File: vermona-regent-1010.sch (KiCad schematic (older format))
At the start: 0 parts

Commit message: Start drawing schematics
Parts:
- added C?: C, symbol Device:C
- added J?: Input, symbol Connector_Generic:Conn_01x02
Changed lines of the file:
@@
 encoding utf-8
 Sheet 1 1
-Title ""
-Date "2021-06-09"
-Rev ""
-Comp ""
+Title "Vermona Regent 1010"
+Date "2021-06-16"
+Rev "0.1"
+Comp "Радиохобби 6/2010"
 Comment1 ""
 Comment2 ""
@@
 Comment4 ""
 $EndDescr
+$Comp
+L Connector_Generic:Conn_01x02 J?
+U 1 1 60C93D53
+P 1200 2800
+F 0 "J?" H 1118 3017 50  0000 C CNN
+F 1 "Input" H 1118 2926 50  0000 C CNN
+F 2 "" H 1200 2800 50  0001 C CNN
+F 3 "~" H 1200 2800 50  0001 C CNN
+	1    1200 2800
+	-1   0    0    -1
+$EndComp
+$Comp
+L Device:C C?
+U 1 1 60C94D66
+P 1850 2800
+F 0 "C?" V 2102 2800 50  0000 C CNN
+F 1 "C" V 2011 2800 50  0000 C CNN
+F 2 "" H 1888 2650 50  0001 C CNN
+F 3 "~" H 1850 2800 50  0001 C CNN
+	1    1850 2800
+	0    -1   -1   0
+$EndComp
 $EndSCHEMATC

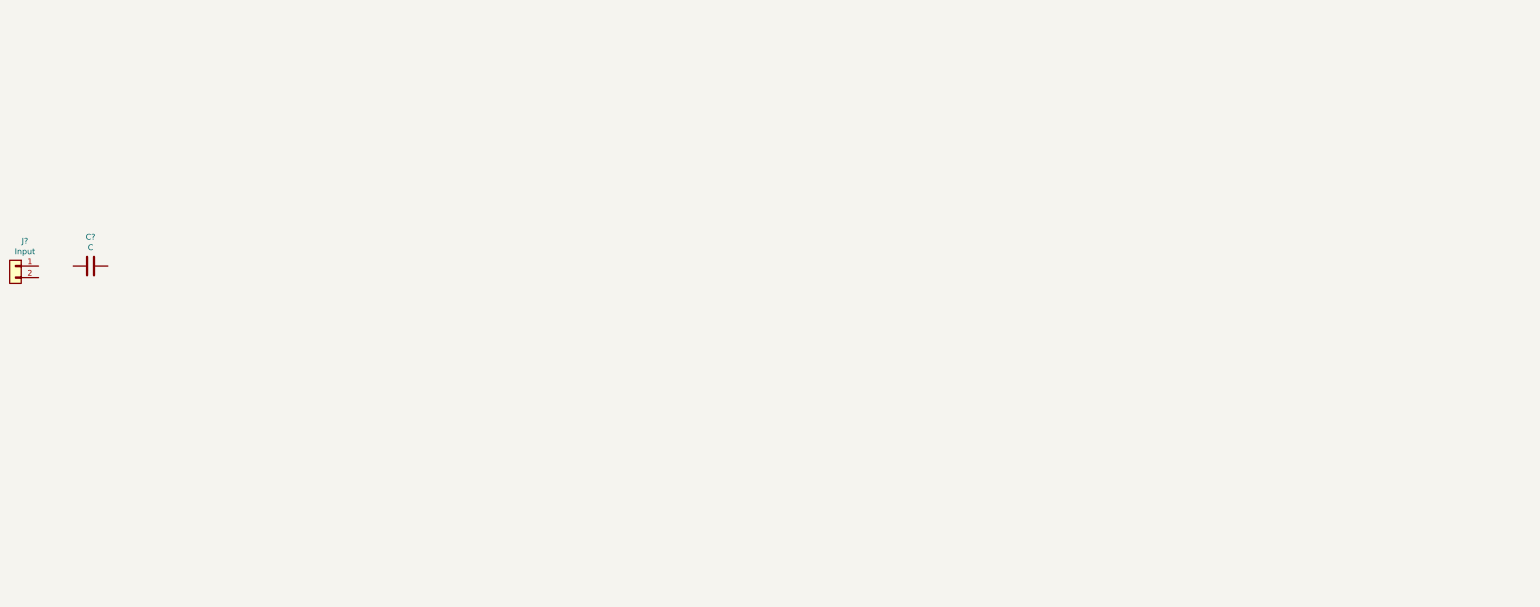
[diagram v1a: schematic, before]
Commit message: Draw lower shoulder
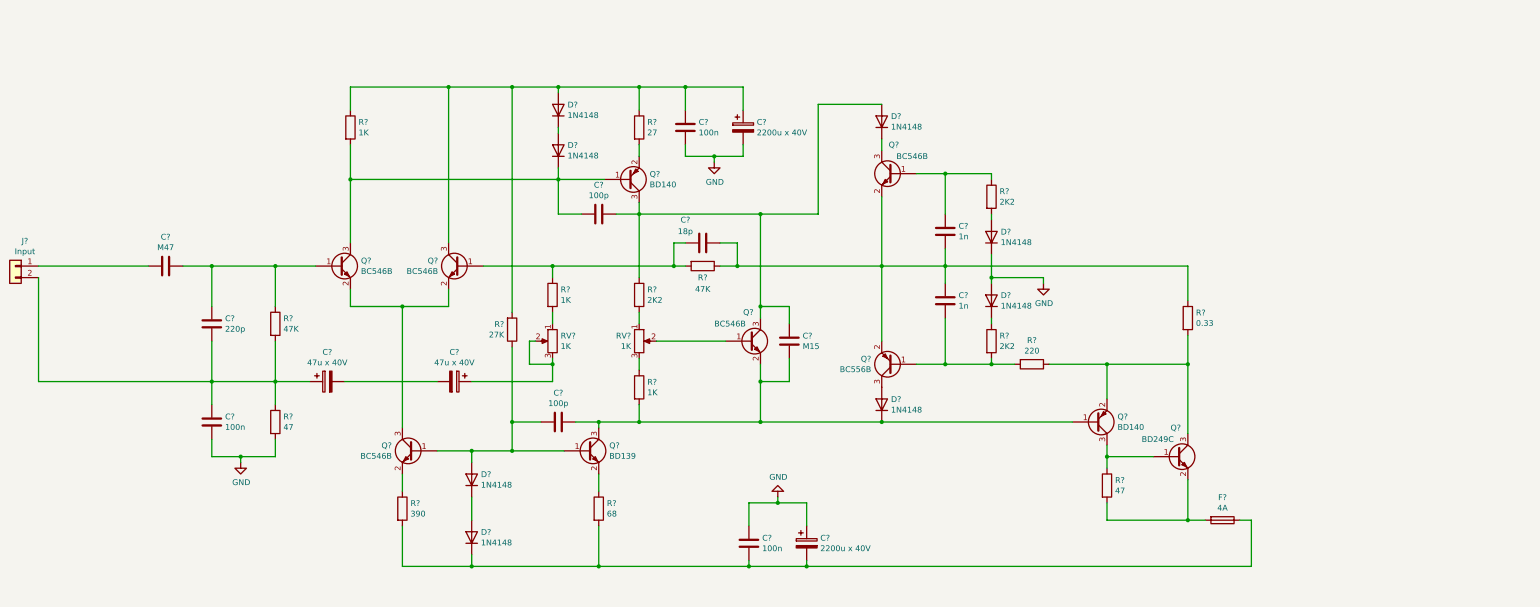
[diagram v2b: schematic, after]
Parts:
- added C?: 220p, symbol Device:C
- added C? (x3): 100n, symbol Device:C
- added C? (x2): 47u x 40V, symbol Device:CP
- added C? (x2): 100p, symbol Device:C
- added C? (x2): 2200u x 40V, symbol Device:CP
- added C?: 18p, symbol Device:C
- added C?: M15, symbol Device:C
- added C? (x2): 1n, symbol Device:C
- added D? (x8): 1N4148, symbol Device:D
- added F?: 4A, symbol Device:Fuse
- added Q? (x5): BC546B, symbol Device:Q_NPN_BEC
- added Q?: BD139, symbol Device:Q_NPN_BEC
- added Q? (x2): BD140, symbol Device:Q_PNP_BEC
- added Q?: BC556B, symbol Device:Q_PNP_BEC
- added Q?: BD249C, symbol Device:Q_NPN_BEC
- added R? (x2): 47K, symbol Device:R
- added R? (x2): 47, symbol Device:R
- added R?: 390, symbol Device:R
- added R? (x3): 1K, symbol Device:R
- added R?: 27K, symbol Device:R
- added R?: 68, symbol Device:R
- added R?: 27, symbol Device:R
- added R? (x3): 2K2, symbol Device:R
- added R?: 220, symbol Device:R
- added R?: 0.33, symbol Device:R
- added RV? (x2): 1K, symbol Device:R_POT
- C?: value C -> M47
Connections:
- net at J?.1 (Pin_1): now also C?.1
- net at J?.2 (Pin_2): now also C?.1, C?.1, C?.2, R?.1, R?.2
- net at C?.2: now also C?.1, Q?.1 (B), R?.1
- new net: Q?.2 (E), Q?.2 (E), Q?.3 (C)
- new net: C?.1, D?.1 (K), Q?.1 (B), Q?.3 (C), R?.2
- new net: C?.2, Q?.1 (B), R?.1, R?.2
- new net: C?.1, C?.1, D?.2 (A), Q?.3 (C), R?.1, R?.1, R?.2
- new net: C?.2, C?.2
- new net: C?.1, RV?.2, RV?.3
- new net: C?.2, D?.2 (A), Q?.1 (B), Q?.1 (B), R?.1
- new net: Q?.2 (E), R?.1 (x2)
- new net: C?.2, C?.2, D?.1 (K), F?.1, R?.2, R?.2
- new net: D?.1 (K), D?.2 (A) (x2)
- new net: C?.1, C?.2, D?.1 (K), Q?.1 (B), Q?.2 (E), Q?.3 (C), R?.2
- new net: R?.2, RV?.1 (x2)
- new net: Q?.2 (E), R?.2
- new net: C?.1, C?.2, D?.2 (A), Q?.3 (C), Q?.3 (C), R?.1
- new net: Q?.1 (B), RV?.2
- new net: R?.1, RV?.3
- new net: C?.1, C?.1, C?.2, Q?.2 (E), Q?.2 (E), R?.1, R?.1
- new net: D?.1 (K), Q?.3 (C)
- new net: C?.1, Q?.1 (B), R?.1
- new net: C?.2, Q?.1 (B), R?.2, R?.2
- new net: D?.2 (A), Q?.3 (C)
- new net: D?.2 (A), R?.2
- new net: D?.1 (K), R?.1
- new net: Q?.2 (E), Q?.3 (C), R?.1, R?.2
- new net: Q?.1 (B), Q?.3 (C), R?.1
- new net: F?.2, Q?.2 (E), R?.2
- new net GND: C?.1, C?.1, C?.2, C?.2, C?.2, D?.1 (K), D?.2 (A), R?.2
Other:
- moved on the sheet: C?

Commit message: Finish schematics
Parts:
- added C16: 100n, symbol Device:C
- added F1: 4A, symbol Device:Fuse
- added LS1: 100W x 4 Ohm, symbol Device:Speaker
- added Q11: КТ819ГМ, symbol Device:Q_NPN_BEC
- added Q9: КТ815Г, symbol Device:Q_NPN_BEC
- added R14: 220, symbol Device:R
- added R16: 47, symbol Device:R
- added R18: 0.33, symbol Device:R
- added R20: 10, symbol Device:R
- Q1, Q2, Q3, Q6, Q7: renamed from Q?; value BC546B -> КТ3102Б
- Q10, Q5: renamed from Q?; value BD140 -> КТ814Г
- Q12: renamed from Q?; value BD249C -> КТ819ГМ
- Q4: renamed from Q?; value BD139 -> КТ815Г
- Q8: renamed from Q?; value BC556B -> КТ502Д
- gave numbers to parts that had none: 43
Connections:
- net GND: now also C16.2, LS1.2
- net at C10.1, C8.1, D3.2 (A)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: now also F1.2, Q11.3 (C), Q9.3 (C)
- net -40V: now reaches C11.2, C13.2, D2.1 (K), F2.1, R4.2, R7.2
- net at C12.1, C7.2, D5.2 (A)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: now also Q9.1 (B)
- net at C14.2, C15.1, C9.1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: now also LS1.1, R18.2, R20.1
- net at C14.1, Q7.1 (B), R12.1: now also R14.2
- new net: Q11.2 (E), R14.1, R16.2, R18.1
- new net: Q11.1 (B), Q9.2 (E), R16.1
- new net: C16.1, R20.2
- new net 40V: F1.1
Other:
- moved on the sheet: C10, C8, D3, D4, D5, R15, R3, R8

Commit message: Trace differential amp
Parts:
- removed C1: M47, symbol Device:C
- removed C12: M15, symbol Device:C
- added C1: 47u x 40V, Capacitor_THT:CP_Radial_D6.3mm_P2.50mm, symbol Device:CP
- added C12: 15u x 40V, Capacitor_THT:CP_Radial_D5.0mm_P2.00mm, symbol Device:CP
- C10, C13: footprint (none) -> Capacitor_THT:CP_Radial_D16.0mm_P7.50mm
- C11, C14, C15, C16, C2, C3, C6, C7, C8: footprint (none) -> Capacitor_THT:C_Rect_L7.0mm_W4.5mm_P5.00mm
- C4, C5: footprint (none) -> Capacitor_THT:CP_Radial_D6.3mm_P2.50mm
- C9: footprint (none) -> Capacitor_THT:C_Rect_L4.6mm_W3.8mm_P2.50mm_MKS02_FKP02
- D1, D2, D3, D4, D5, D6, D7, D8: value 1N4148 -> КД522Б; footprint (none) -> Diode_THT:D_DO-15_P15.24mm_Horizontal
- F1, F2: footprint (none) -> Fuse:Fuseholder_Cylinder-5x20mm_Stelvio-Kontek_PTF78_Horizontal_Open
- J1, LS1: footprint (none) -> Connector_PinHeader_2.54mm:PinHeader_1x02_P2.54mm_Vertical
- Q1, Q2, Q3, Q6, Q7, Q8: footprint (none) -> Package_TO_SOT_THT:TO-92
- Q10, Q4, Q5, Q9: footprint (none) -> Package_TO_SOT_THT:TO-126-3_Vertical
- Q11, Q12: value КТ819ГМ -> КТ808; footprint (none) -> Connector_PinHeader_2.54mm:PinHeader_1x03_P2.54mm_Vertical
- R1, R10, R11, R12, R13, R14, R15, R16, R17, R2, R20, R3, R4, R5, R6, R7, R8, R9: footprint (none) -> Resistor_THT:R_Axial_DIN0309_L9.0mm_D3.2mm_P12.70mm_Horizontal
- R18, R19: footprint (none) -> Resistor_THT:R_Axial_DIN0414_L11.9mm_D4.5mm_P20.32mm_Horizontal
- RV1, RV2: footprint (none) -> Potentiometer_THT:Potentiometer_Piher_PT-10-V10_Vertical
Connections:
- net 40V: now also C10.1, C8.1, D3.2 (A), Q3.3 (C), R3.1, R5.2, R8.1
- net at J1.1 (Pin_1): now also C1.1
- net at C2.1, Q1.1 (B), R1.1: now also C1.2
- net at C6.1, D6.1 (K), Q10.1 (B)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: now also C12.2
- net at C7.2, D5.2 (A), Q5.3 (C)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: now also C12.1
- new net: F1.2, Q11.3 (C), Q9.3 (C)
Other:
- moved on the sheet: C10, C7, C8, D3, D4, F1, Q5, R3, R8

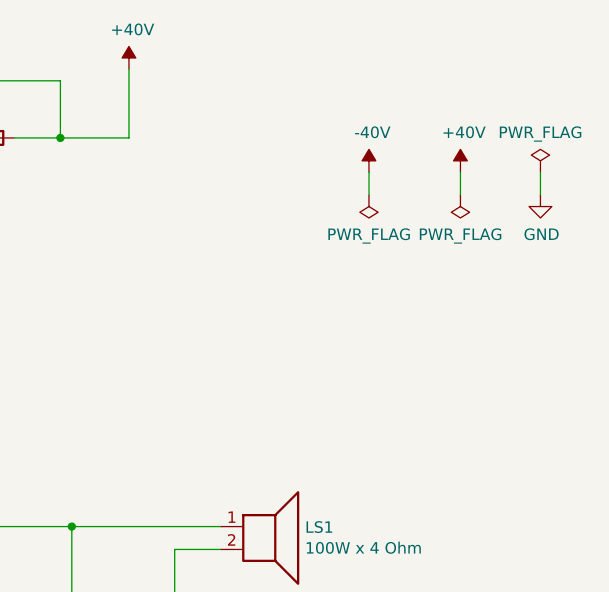
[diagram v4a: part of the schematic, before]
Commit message: Finish routing amp
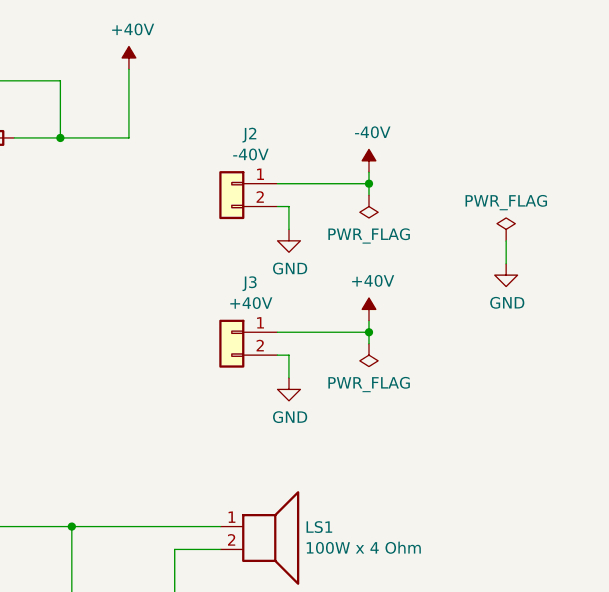
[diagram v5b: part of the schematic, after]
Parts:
- added J2: -40V, Connector_PinHeader_2.54mm:PinHeader_1x02_P2.54mm_Vertical, symbol Connector_Generic:Conn_01x02
- added J3: +40V, Connector_PinHeader_2.54mm:PinHeader_1x02_P2.54mm_Vertical, symbol Connector_Generic:Conn_01x02
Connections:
- net -40V: now also J2.1 (Pin_1)
- net 40V: now also J3.1 (Pin_1)
- net GND: now also J2.2 (Pin_2), J3.2 (Pin_2)
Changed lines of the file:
@@
 L component:+40V #PWR013
 U 1 1 60E0CA4A
-P 13750 1250
-F 0 "#PWR013" H 13750 1350 50  0001 C CNN
-F 1 "+40V" H 13765 1423 50  0000 C CNN
-F 2 "" H 13750 1250 50  0001 C CNN
-F 3 "" H 13750 1250 50  0001 C CNN
-	1    13750 1250
+P 13350 1900
+F 0 "#PWR013" H 13350 2000 50  0001 C CNN
+F 1 "+40V" H 13365 2073 50  0000 C CNN
+F 2 "" H 13350 1900 50  0001 C CNN
+F 3 "" H 13350 1900 50  0001 C CNN
+	1    13350 1900
 	1    0    0    -1
 $EndComp
@@
 L power:GND #PWR014
 U 1 1 60E0D3DC
-P 14100 1350
-F 0 "#PWR014" H 14100 1100 50  0001 C CNN
-F 1 "GND" H 14105 1177 50  0000 C CNN
-F 2 "" H 14100 1350 50  0001 C CNN
-F 3 "" H 14100 1350 50  0001 C CNN
-	1    14100 1350
+P 13950 1650
+F 0 "#PWR014" H 13950 1400 50  0001 C CNN
+F 1 "GND" H 13955 1477 50  0000 C CNN
+F 2 "" H 13950 1650 50  0001 C CNN
+F 3 "" H 13950 1650 50  0001 C CNN
+	1    13950 1650
 	1    0    0    -1
 $EndComp
@@
 L power:PWR_FLAG #FLG02
 U 1 1 60CFE24B
-P 13750 1350
-F 0 "#FLG02" H 13750 1425 50  0001 C CNN
-F 1 "PWR_FLAG" H 13750 1523 50  0000 C CNN
-F 2 "" H 13750 1350 50  0001 C CNN
-F 3 "~" H 13750 1350 50  0001 C CNN
-	1    13750 1350
+P 13350 2000
+F 0 "#FLG02" H 13350 2075 50  0001 C CNN
+F 1 "PWR_FLAG" H 13350 2173 50  0000 C CNN
+F 2 "" H 13350 2000 50  0001 C CNN
+F 3 "~" H 13350 2000 50  0001 C CNN
+	1    13350 2000
 	-1   0    0    1
 $EndComp
-Wire Wire Line
-	13750 1250 13750 1350
 $Comp
 L power:PWR_FLAG #FLG01
@@
 $EndComp
 Wire Wire Line
-	13350 1250 13350 1350
+	13350 1250 13350 1300
 $Comp
 L power:PWR_FLAG #FLG03
 U 1 1 60D1985F
-P 14100 1250
-F 0 "#FLG03" H 14100 1325 50  0001 C CNN
-F 1 "PWR_FLAG" H 14100 1423 50  0000 C CNN
-F 2 "" H 14100 1250 50  0001 C CNN
-F 3 "~" H 14100 1250 50  0001 C CNN
-	1    14100 1250
-	1    0    0    -1
-$EndComp
-Wire Wire Line
-	14100 1250 14100 1350
+P 13950 1550
+F 0 "#FLG03" H 13950 1625 50  0001 C CNN
+F 1 "PWR_FLAG" H 13950 1723 50  0000 C CNN
+F 2 "" H 13950 1550 50  0001 C CNN
+F 3 "~" H 13950 1550 50  0001 C CNN
+	1    13950 1550
+	1    0    0    -1
+$EndComp
+Wire Wire Line
+	13950 1550 13950 1650
 $Comp
 L Device:CP C1
@@
 Wire Wire Line
 	12000 1100 11800 1100
+$Comp
+L Connector_Generic:Conn_01x02 J2
+U 1 1 60DCBF3A
+P 12750 1300
+F 0 "J2" H 12668 1517 50  0000 C CNN
+F 1 "-40V" H 12668 1426 50  0000 C CNN
+F 2 "Connector_PinHeader_2.54mm:PinHeader_1x02_P2.54mm_Vertical" H 12750 1300 50  0001 C CNN
+F 3 "~" H 12750 1300 50  0001 C CNN
+	1    12750 1300
+	-1   0    0    -1
+$EndComp
+Wire Wire Line
+	12950 1300 13350 1300
+Connection ~ 13350 1300
+Wire Wire Line
+	13350 1300 13350 1350
+$Comp
+L power:GND #PWR015
+U 1 1 60DE5D3F
+P 13000 1500
+F 0 "#PWR015" H 13000 1250 50  0001 C CNN
+F 1 "GND" H 13005 1327 50  0000 C CNN
+F 2 "" H 13000 1500 50  0001 C CNN
+F 3 "" H 13000 1500 50  0001 C CNN
+	1    13000 1500
+	1    0    0    -1
+$EndComp
+Wire Wire Line
+	12950 1400 13000 1400
+Wire Wire Line
+	13000 1400 13000 1500
+$Comp
+L Connector_Generic:Conn_01x02 J3
+U 1 1 60E015D2
+P 12750 1950
+F 0 "J3" H 12668 2167 50  0000 C CNN
+F 1 "+40V" H 12668 2076 50  0000 C CNN
+F 2 "Connector_PinHeader_2.54mm:PinHeader_1x02_P2.54mm_Vertical" H 12750 1950 50  0001 C CNN
+F 3 "~" H 12750 1950 50  0001 C CNN
+	1    12750 1950
+	-1   0    0    -1
+$EndComp
+$Comp
+L power:GND #PWR016
+U 1 1 60E015D9
+P 13000 2150
+F 0 "#PWR016" H 13000 1900 50  0001 C CNN
+F 1 "GND" H 13005 1977 50  0000 C CNN
+F 2 "" H 13000 2150 50  0001 C CNN
+F 3 "" H 13000 2150 50  0001 C CNN
+	1    13000 2150
+	1    0    0    -1
+$EndComp
+Wire Wire Line
+	12950 2050 13000 2050
+Wire Wire Line
+	13000 2050 13000 2150
+Wire Wire Line
+	13350 1900 13350 1950
+Wire Wire Line
+	12950 1950 13350 1950
+Connection ~ 13350 1950
+Wire Wire Line
+	13350 1950 13350 2000
 $EndSCHEMATC
